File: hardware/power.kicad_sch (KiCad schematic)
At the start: 15 parts, among them J16 LOGIC 12-48V, J17 12V_LINK, Q1 IRF9540N, U5 D36V50F5, U6 D36V50F12

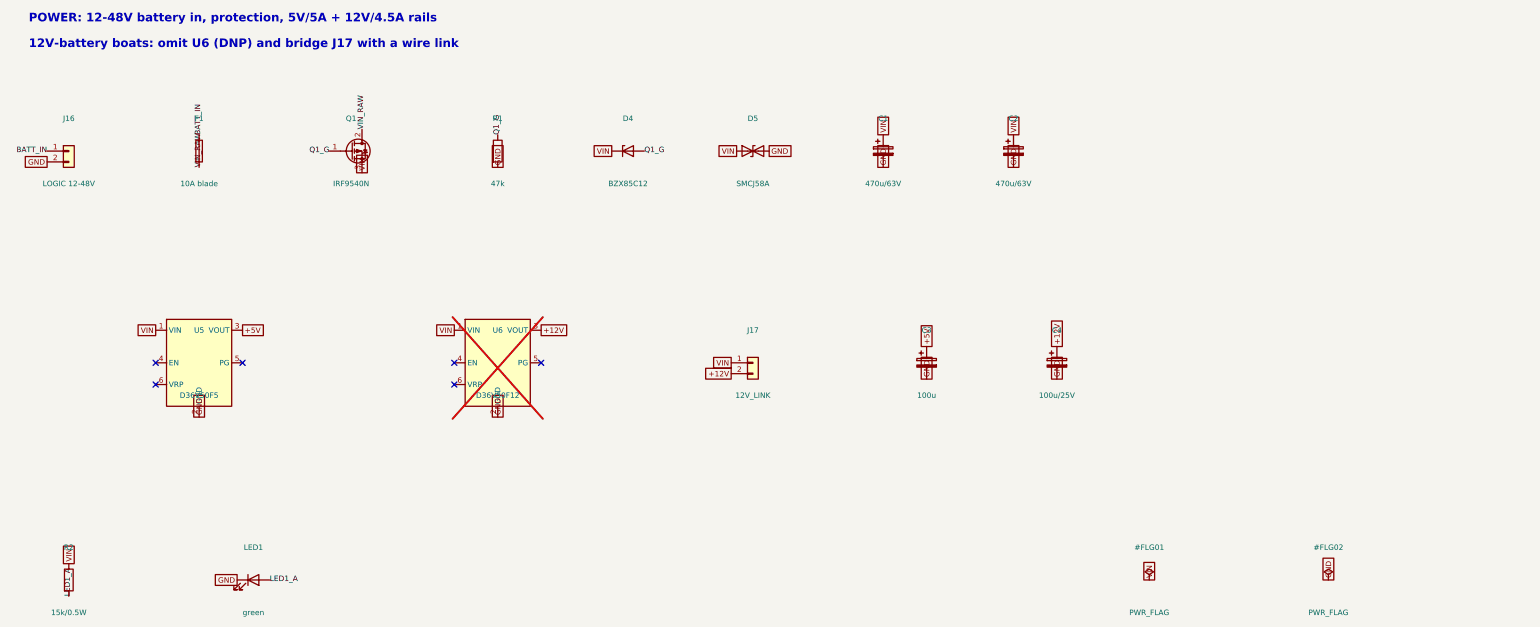
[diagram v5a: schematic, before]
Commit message: feat: v3.1 12V-only — generic 5V buck module on J14, U5/U6/J17 removed, SMCJ18A TVS, servo direct on VIN; DRC clean
Co-Authored-By: Claude Fable 5 <noreply@anthropic.com>
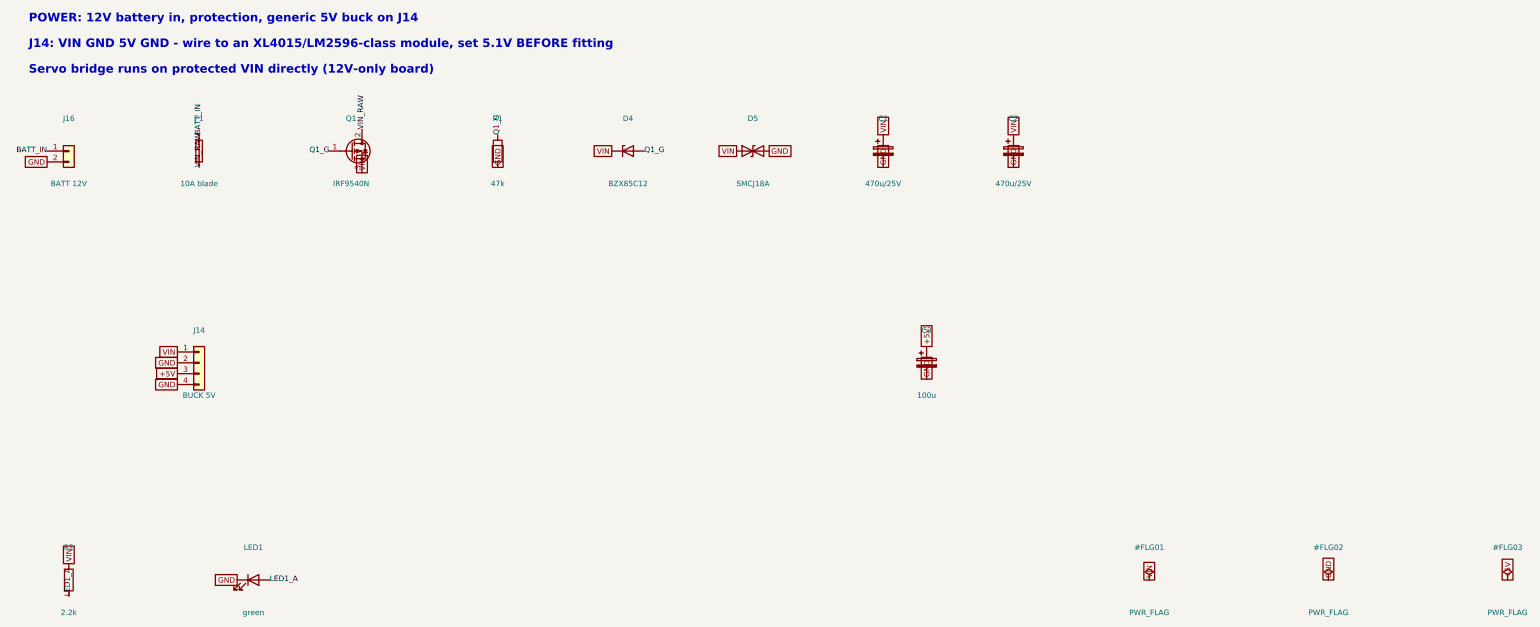
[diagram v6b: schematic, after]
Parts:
- removed C4: 100u/25V, Capacitor_THT:CP_Radial_D6.3mm_P2.50mm, symbol Device:C_Polarized
- removed J17: 12V_LINK, TerminalBlock_CUI:TerminalBlock_CUI_TB007-508-02_1x02_P5.08mm_Horizontal, symbol Connector_Generic:Conn_01x02
- removed U5: D36V50F5, vanchor-helm:Pololu_D36V50Fx, symbol vanchor-helm:D36V50Fx
- removed U6: D36V50F12, vanchor-helm:Pololu_D36V50Fx, symbol vanchor-helm:D36V50Fx
- added J14: BUCK 5V, Connector_PinHeader_2.54mm:PinHeader_1x04_P2.54mm_Vertical, symbol Connector_Generic:Conn_01x04
- C1, C2: value 470u/63V -> 470u/25V; MPN EEU-FR1J471B -> EEU-FR1E471B
- D5: value SMCJ58A -> SMCJ18A; MPN SMCJ58A -> SMCJ18A
- J16: value LOGIC 12-48V -> BATT 12V
- R2: value 15k/0.5W -> 2.2k
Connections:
- net +5V: now also J14.3 (Pin_3)
- net GND: now also J14.2 (Pin_2), J14.4 (Pin_4)
- net VIN: now also J14.1 (Pin_1)
- no-connect marks 6 -> 0
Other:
- note added: "J14: VIN GND 5V GND - wire to an XL4015/LM2596-class module, set 5.1V BEFORE fitting"
- note added: "POWER: 12V battery in, protection, generic 5V buck on J14"
- note added: "Servo bridge runs on protected VIN directly (12V-only board)"
- note removed: "12V-battery boats: omit U6 (DNP) and bridge J17 with a wire link"
- note removed: "POWER: 12-48V battery in, protection, 5V/5A + 12V/4.5A rails"
